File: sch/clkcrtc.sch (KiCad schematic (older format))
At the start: 26 parts, among them Q1 16 MHz, Q2 13.333 MHz

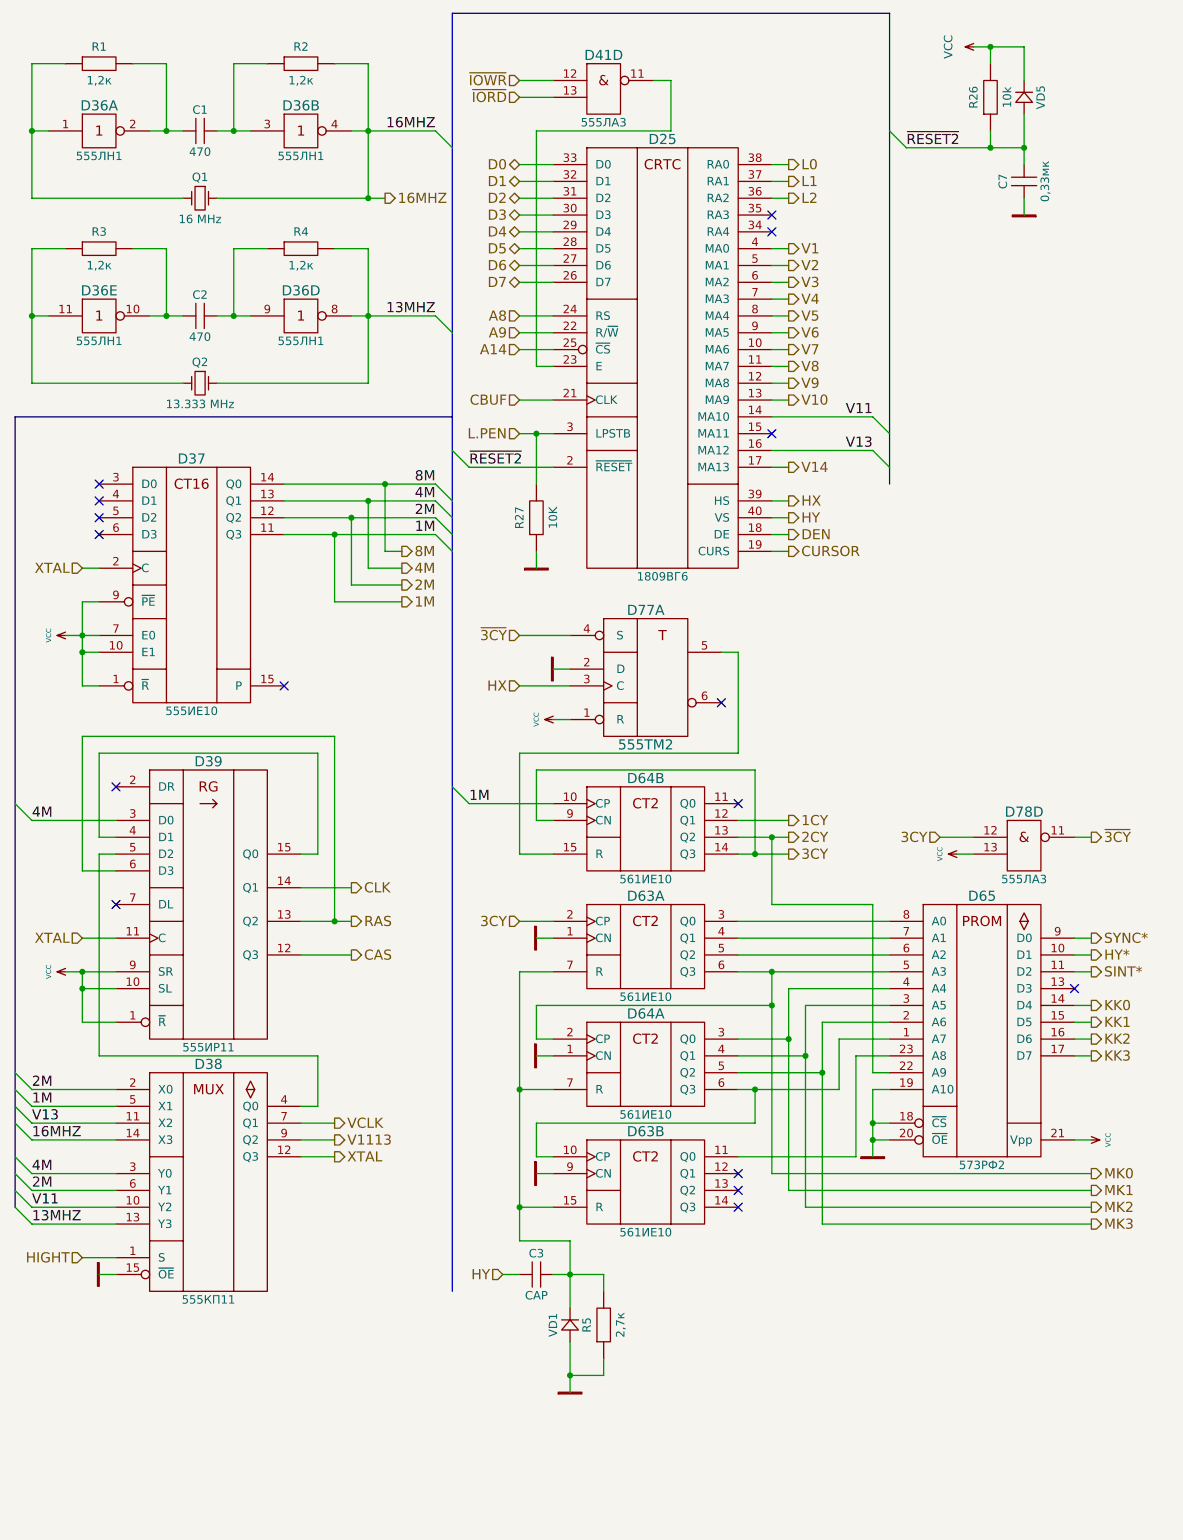
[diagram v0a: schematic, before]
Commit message: Start to move to a bit more affordable components
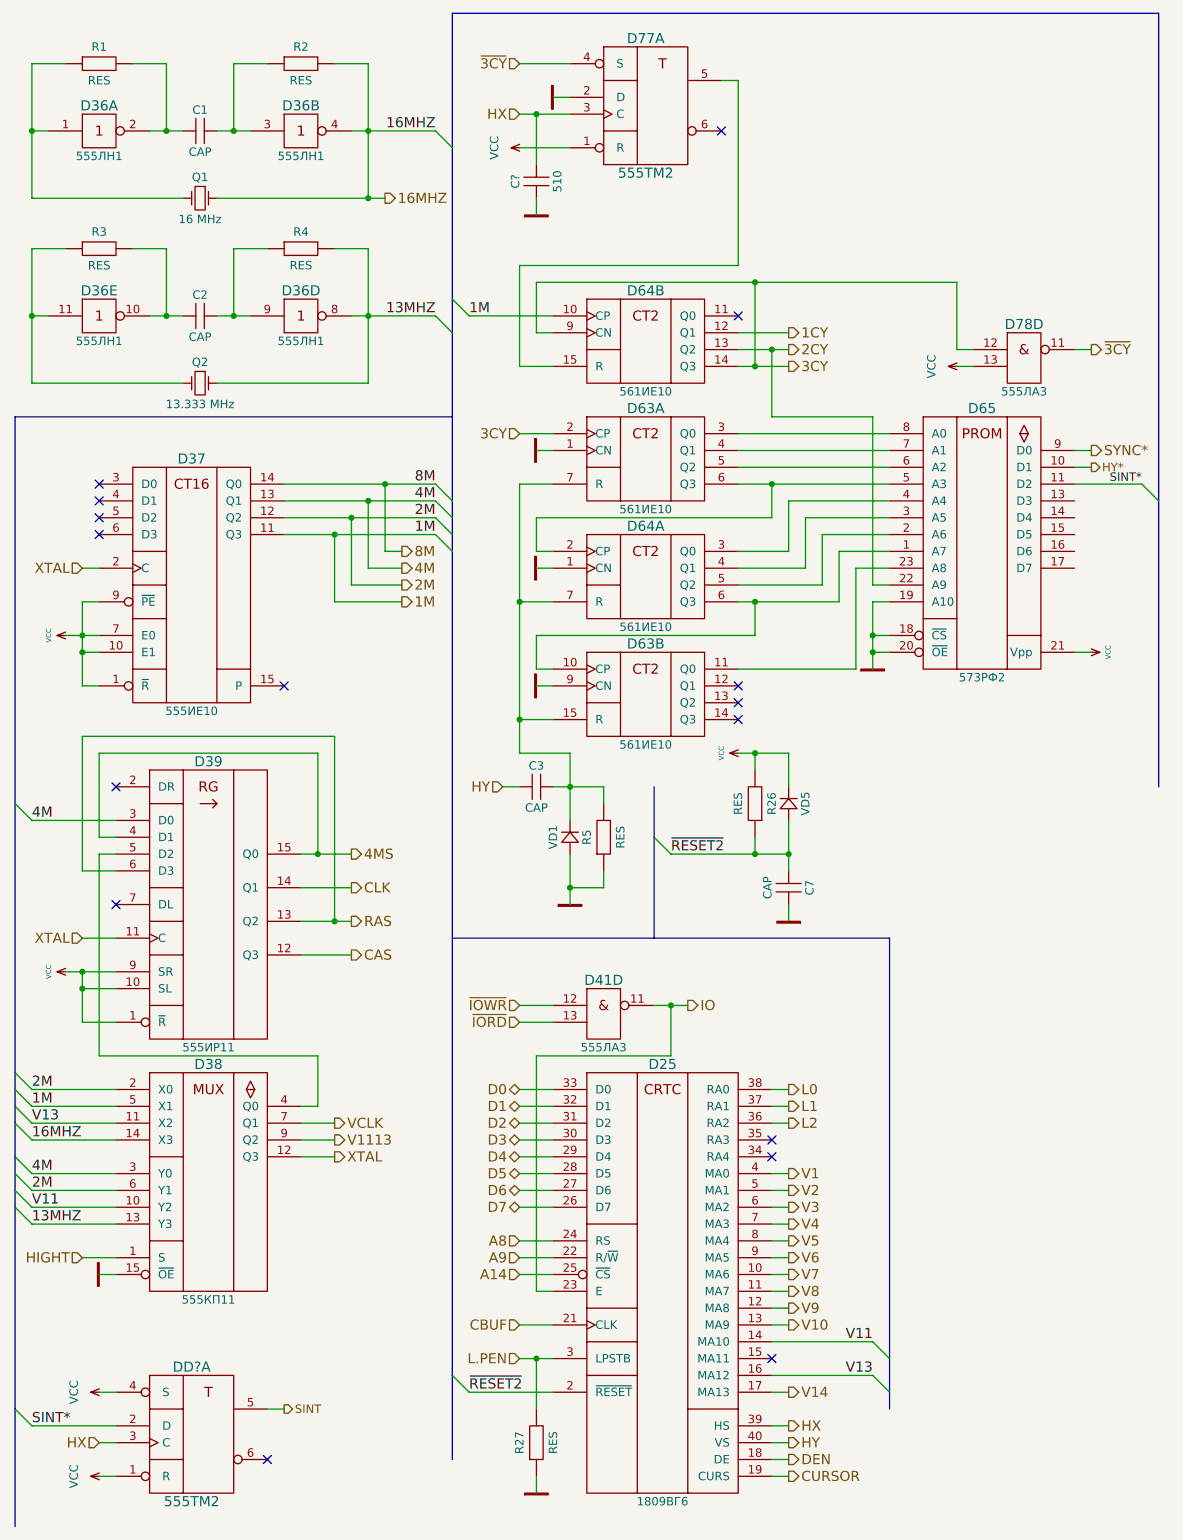
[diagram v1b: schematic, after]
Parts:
- added C?: 510, symbol CAP
- added DD?: 555ТМ2, symbol 555ТМ2
- C1, C2: value 470 -> CAP
- C7: value 0,33мк -> CAP
- R1, R2, R3, R4: value 1,2к -> RES
- R26: value 10k -> RES
- R27: value 10K -> RES
- R5: value 2,7к -> RES
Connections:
- net GND: now also C?.1, DD?.7 (GND)
- net HX: now also C?.2, DD?.3 (C)
- net SINT*: now also DD?.2 (D)
- net VCC: now also DD?.1 (R), DD?.14 (VCC), DD?.4 (S)
- net IO: now reaches D25.23 (E), D41.11 (out)
- net 4MS: now reaches D39.15 (Q0), D39.4 (D1)
- net KK0: no longer names the net of D65.14 (D4)
- net KK1: no longer names the net of D65.15 (D5)
- net KK2: no longer names the net of D65.16 (D6)
- net KK3: no longer names the net of D65.17 (D7)
- net MK0: no longer names the net of D63.6 (Q3), D64.2 (CP), D65.5 (A3)
- net MK1: no longer names the net of D64.3 (Q0), D65.4 (A4)
- net MK2: no longer names the net of D64.4 (Q1), D65.3 (A5)
- net MK3: no longer names the net of D64.5 (Q2), D65.2 (A6)
- new net SINT: DD?.5
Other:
- moved on the sheet: C3, C7, D25, D41D, D63A, D63B, D64A, D64B, D65, D77A, D78D, R26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

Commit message: Another ROM replaced with PLD, source included
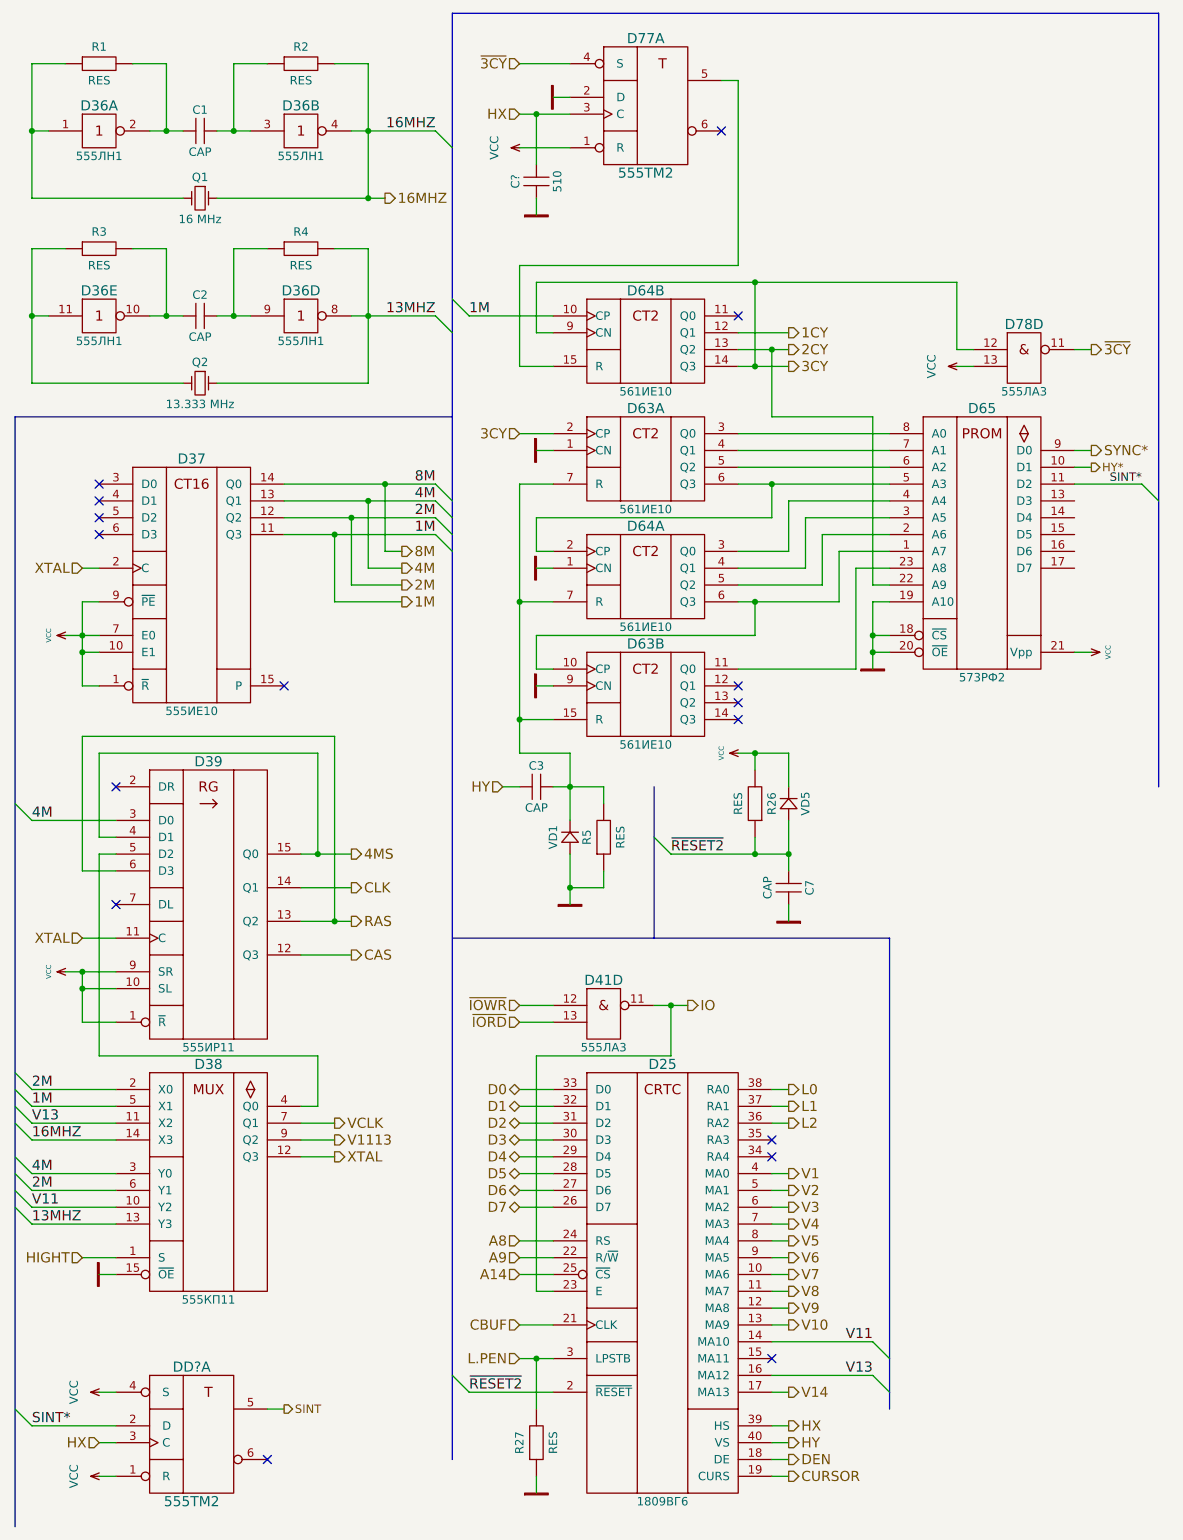
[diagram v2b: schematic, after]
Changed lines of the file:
@@
 EESchema Schematic File Version 2
-LIBS:aleste-rescue
 LIBS:mylib
 LIBS:power
@@
 V13
 Wire Wire Line
-	1600 1500 1700 1500
-Wire Wire Line
-	1700 1500 1800 1500
-Wire Wire Line
-	2000 1500 2100 1500
-Wire Wire Line
-	2100 1500 2200 1500
+	1600 1500 1800 1500
+Wire Wire Line
+	2000 1500 2200 1500
 Wire Wire Line
 	2300 1100 2100 1100
@@
 	1100 1100 900  1100
 Wire Wire Line
-	900  1100 900  1500
-Wire Wire Line
-	900  1500 900  1900
+	900  1100 900  1900
 Wire Wire Line
 	900  1500 1000 1500
@@
 	2700 1100 2900 1100
 Wire Wire Line
-	2900 1100 2900 1500
-Wire Wire Line
-	2900 1500 2900 1900
-Wire Wire Line
-	2800 1500 2900 1500
-Wire Wire Line
-	2900 1500 3300 1500
-Wire Wire Line
-	2000 1900 2900 1900
-Wire Wire Line
-	2900 1900 3000 1900
+	2900 1100 2900 1900
+Wire Wire Line
+	2800 1500 3300 1500
+Wire Wire Line
+	2000 1900 3000 1900
 Connection ~ 2900 1500
 Wire Wire Line
@@
 	1100 2200 900  2200
 Wire Wire Line
-	900  2200 900  2600
-Wire Wire Line
-	900  2600 900  3000
+	900  2200 900  3000
 Wire Wire Line
 	2700 2200 2900 2200
 Wire Wire Line
-	2900 2200 2900 2600
-Wire Wire Line
-	2900 2600 2900 3000
-Wire Wire Line
-	1600 2600 1700 2600
-Wire Wire Line
-	1700 2600 1800 2600
-Wire Wire Line
-	2000 2600 2100 2600
-Wire Wire Line
-	2100 2600 2200 2600
+	2900 2200 2900 3000
+Wire Wire Line
+	1600 2600 1800 2600
+Wire Wire Line
+	2000 2600 2200 2600
 Connection ~ 2100 2600
 Wire Wire Line
@@
 	900  2600 1000 2600
 Wire Wire Line
-	2800 2600 2900 2600
-Wire Wire Line
-	2900 2600 3300 2600
+	2800 2600 3300 2600
 Wire Wire Line
 	2900 3000 2000 3000
@@
 	1300 4300 1200 4300
 Wire Wire Line
-	1200 4300 1200 4500
-Wire Wire Line
-	1200 4500 1200 4600
-Wire Wire Line
-	1200 4600 1200 4800
+	1200 4300 1200 4800
 Wire Wire Line
 	1200 4800 1300 4800
@@
 Connection ~ 1200 4600
 Wire Wire Line
-	1100 4500 1200 4500
-Wire Wire Line
-	1200 4500 1300 4500
+	1100 4500 1300 4500
 Connection ~ 1200 4500
 Wire Wire Line
-	2400 3600 3000 3600
-Wire Wire Line
-	3000 3600 3300 3600
-Wire Wire Line
-	2400 3700 2900 3700
-Wire Wire Line
-	2900 3700 3300 3700
-Wire Wire Line
-	2400 3800 2800 3800
-Wire Wire Line
-	2800 3800 3300 3800
-Wire Wire Line
-	2400 3900 2700 3900
-Wire Wire Line
-	2700 3900 3300 3900
+	2400 3600 3300 3600
+Wire Wire Line
+	2400 3700 3300 3700
+Wire Wire Line
+	2400 3800 3300 3800
+Wire Wire Line
+	2400 3900 3300 3900
 Wire Wire Line
 	900  7200 1400 7200
@@
 	3900 2700 3900 2400
 Wire Wire Line
-	3900 2400 5200 2400
-Wire Wire Line
-	5200 2400 6400 2400
+	3900 2400 6400 2400
 Wire Wire Line
 	5200 2400 5200 2900
 Wire Wire Line
-	5100 2900 5200 2900
-Wire Wire Line
-	5200 2900 5400 2900
+	5100 2900 5400 2900
 Wire Wire Line
 	5100 2700 5400 2700
 Wire Wire Line
-	5100 2800 5300 2800
-Wire Wire Line
-	5300 2800 5400 2800
+	5100 2800 5400 2800
 Connection ~ 5200 2900
 Wire Wire Line
-	5100 3600 5300 3600
-Wire Wire Line
-	5300 3600 6000 3600
+	5100 3600 6000 3600
 Wire Wire Line
 	3900 3800 3900 4000
@@
 	5200 4500 5200 4300
 Wire Wire Line
-	5100 4300 5200 4300
-Wire Wire Line
-	5200 4300 5700 4300
+	5100 4300 5700 4300
 Wire Wire Line
 	3800 5000 4000 5000
 Wire Wire Line
-	3800 3600 3800 4300
-Wire Wire Line
-	3800 4300 3800 5000
-Wire Wire Line
-	3800 5000 3800 5200
+	3800 3600 3800 5200
 Wire Wire Line
 	3800 3600 4000 3600
@@
 	6000 4300 5900 4300
 Wire Wire Line
-	5900 4300 5900 4500
-Wire Wire Line
-	5900 4500 5900 4600
-Wire Wire Line
-	5900 4600 5900 4700
+	5900 4300 5900 4700
 Wire Wire Line
 	6000 4600 5900 4600
@@
 	4300 5400 4300 5500
 Wire Wire Line
-	4000 5400 4100 5400
-Wire Wire Line
-	4100 5400 4300 5400
+	4000 5400 4300 5400
 Wire Wire Line
 	4300 5900 4300 6000
@@
 	4300 6000 4100 6000
 Wire Wire Line
-	4100 5800 4100 6000
-Wire Wire Line
-	4100 6000 4100 6100
-Wire Wire Line
-	4100 5200 4100 5400
-Wire Wire Line
-	4100 5400 4100 5600
+	4100 5800 4100 6100
+Wire Wire Line
+	4100 5200 4100 5600
 Connection ~ 4100 5400
 Connection ~ 4100 6000
@@
 	1300 5800 1400 5800
 Wire Wire Line
-	2500 5800 2600 5800
-Wire Wire Line
-	2600 5800 2800 5800
+	2500 5800 2800 5800
 Wire Wire Line
 	2600 5800 2600 5200
@@
 	2700 5100 2700 6200
 Wire Wire Line
-	2500 6200 2700 6200
-Wire Wire Line
-	2700 6200 2800 6200
+	2500 6200 2800 6200
 Connection ~ 2700 6200
 Wire Wire Line
@@
 	1400 5600 900  5600
 Wire Wire Line
-	1100 6500 1200 6500
-Wire Wire Line
-	1200 6500 1400 6500
-Wire Wire Line
-	1200 6500 1200 6600
-Wire Wire Line
-	1200 6600 1200 6800
+	1100 6500 1400 6500
+Wire Wire Line
+	1200 6500 1200 6800
 Wire Wire Line
 	1200 6800 1400 6800
@@
 	3500 9000 4000 9000
 Wire Wire Line
-	3800 8800 3900 8800
-Wire Wire Line
-	3900 8800 4000 8800
+	3800 8800 4000 8800
 Wire Wire Line
 	3800 8600 4000 8600
@@
 	5400 9500 5300 9500
 Wire Wire Line
-	4600 6700 4700 6700
-Wire Wire Line
-	4700 6700 4800 6700
+	4600 6700 4800 6700
 Wire Wire Line
 	4700 6700 4700 7000
@@
 	3700 5400 3800 5400
 Wire Wire Line
-	3800 1400 3900 1400
-Wire Wire Line
-	3900 1400 4100 1400
+	3800 1400 4100 1400
 Connection ~ 5300 2800
 Wire Wire Line
@@
 Connection ~ 3000 3600
 Wire Wire Line
-	5400 5600 5400 5800
-Wire Wire Line
-	5400 5800 5400 5900
+	5400 5600 5400 5900
 Wire Wire Line
 	5200 5700 5200 5800
 Wire Wire Line
-	4700 5800 5200 5800
-Wire Wire Line
-	5200 5800 5400 5800
+	4700 5800 5400 5800
 Connection ~ 5400 5800
 Wire Wire Line
 	5400 5200 5400 5400
 Wire Wire Line
-	5100 5200 5200 5200
-Wire Wire Line
-	5200 5200 5400 5200
+	5100 5200 5400 5200
 Wire Wire Line
 	5200 5200 5200 5300
@@
 	3900 9600 3900 9500
 Wire Bus Line
-	800  3200 800  5500
-Wire Bus Line
-	800  5500 800  7100
-Wire Bus Line
-	800  7100 800  7200
-Wire Bus Line
-	800  7200 800  7300
-Wire Bus Line
-	800  7300 800  7400
-Wire Bus Line
-	800  7400 800  7600
-Wire Bus Line
-	800  7600 800  7700
-Wire Bus Line
-	800  7700 800  7800
-Wire Bus Line
-	800  7800 800  7900
-Wire Bus Line
-	800  7900 800  9100
-Wire Bus Line
-	800  9100 800  9800
+	800  3200 800  9800
 Wire Bus Line
 	800  3200 3400 3200
 Wire Bus Line
-	3400 800  3400 1600
-Wire Bus Line
-	3400 1600 3400 2500
-Wire Bus Line
-	3400 2500 3400 2700
-Wire Bus Line
-	3400 2700 3400 3700
-Wire Bus Line
-	3400 3700 3400 3800
-Wire Bus Line
-	3400 3800 3400 3900
-Wire Bus Line
-	3400 3900 3400 4000
-Wire Bus Line
-	3400 4000 3400 8900
-Wire Bus Line
-	3400 8900 3400 9400
+	3400 800  3400 9400
 Entry Wire Line
 	800  7800 900  7900
@@
 	3400 800  7600 800
 Wire Bus Line
-	6000 6300 6000 8800
-Wire Bus Line
-	6000 8800 6000 9000
-Wire Bus Line
-	6000 9000 6000 9100
+	6000 6300 6000 9100
 Entry Wire Line
 	5900 8700 6000 8800
@@
 SINT*
 Wire Bus Line
-	7600 800  7600 3700
-Wire Bus Line
-	7600 3700 7600 5400
+	7600 800  7600 5400
 Wire Bus Line
 	6000 6300 3400 6300
 Wire Bus Line
-	4600 5400 4600 5700
-Wire Bus Line
-	4600 5700 4600 6300
+	4600 5400 4600 6300
 Entry Wire Line
 	800  9100 900  9200
